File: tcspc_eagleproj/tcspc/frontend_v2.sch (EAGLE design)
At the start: 11 parts, among them U1 AD8465, X1 SMA

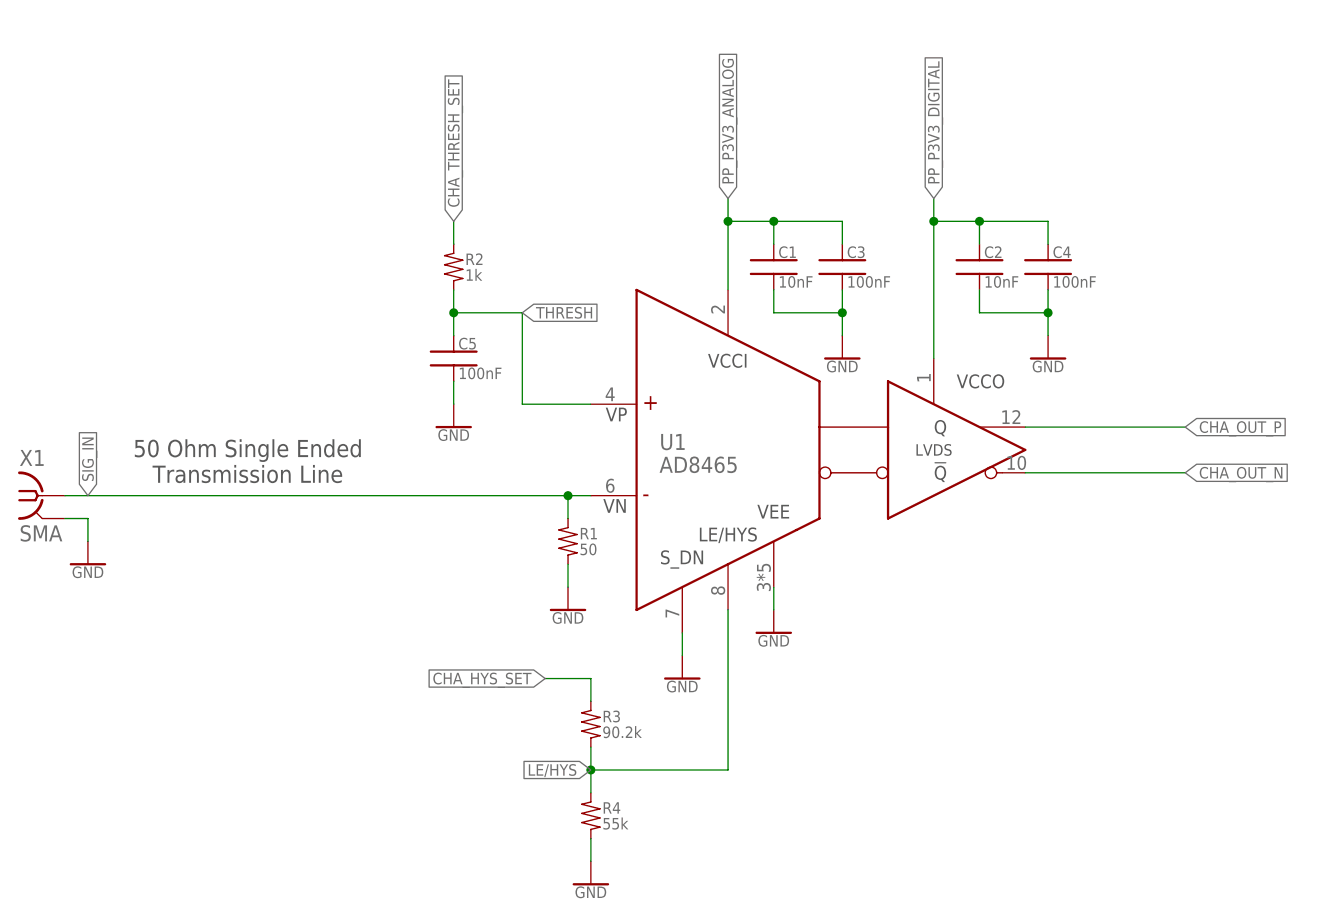
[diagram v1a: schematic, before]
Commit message: small tweaks to the dbl so that I could start putting four of them onto the main board, and then I did just that.
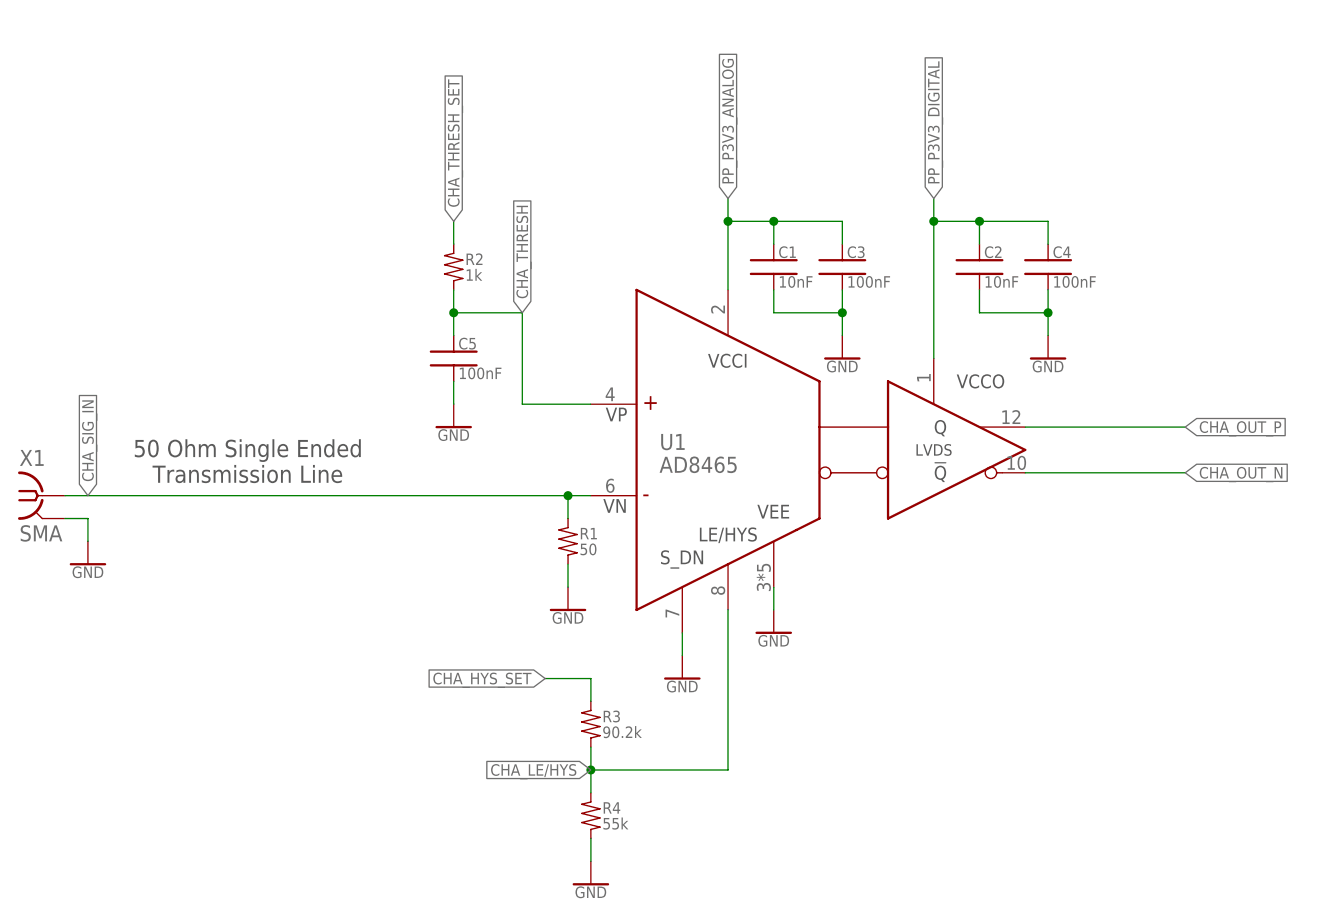
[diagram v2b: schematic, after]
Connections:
- net LE/HYS renamed CHA_LE/HYS
- net SIG_IN renamed CHA_SIG_IN
- net THRESH renamed CHA_THRESH
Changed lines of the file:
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@@
 </segment>
 </net>
-<net name="SIG_IN" class="0">
+<net name="CHA_SIG_IN" class="0">
 <segment>
 <pinref part="U1" gate="G$1" pin="VN"/>
@@
 </segment>
 </net>
-<net name="THRESH" class="0">
+<net name="CHA_THRESH" class="0">
 <segment>
 <pinref part="U1" gate="G$1" pin="VP"/>
 <wire x1="106.68" y1="116.84" x2="99.06" y2="116.84" width="0.1524" layer="91"/>
-<label x="99.06" y="127" size="1.27" layer="95" xref="yes"/>
+<label x="99.06" y="127" size="1.27" layer="95" rot="R90" xref="yes"/>
 <wire x1="99.06" y1="116.84" x2="99.06" y2="127" width="0.1524" layer="91"/>
 <pinref part="C5" gate="G$1" pin="1"/>
@@
 </segment>
 </net>
-<net name="LE/HYS" class="0">
+<net name="CHA_LE/HYS" class="0">
 <segment>
 <pinref part="R3" gate="G$1" pin="2"/>
